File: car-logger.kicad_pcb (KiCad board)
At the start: 4 copper layers, 86.4 x 53.8 mm, 92 parts, among them J1 DB9_Male, J2 Conn_01x05, J3 USB_B_Micro, Q1 Q_NMOS_DGS, SW1 SW_Push, U1 STM32F042C6Tx, U2 S25FLxS, U3 TC122x, U4 MIC5504-3.3YM5, U5 TPS2662x, U6 TPS2662x, U7 TPS5516x-Q1, U8 ISOW1044, Y1 Crystal_GND24_Small

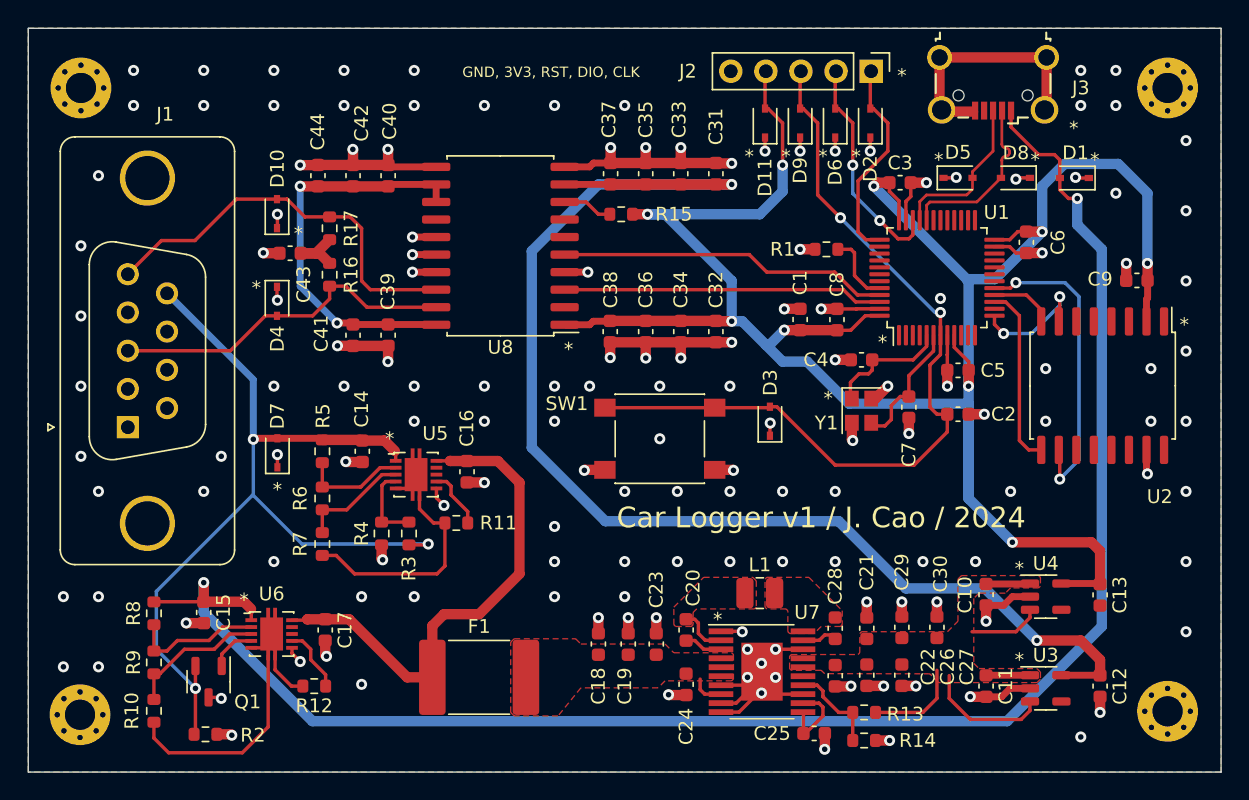
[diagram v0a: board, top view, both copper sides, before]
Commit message: Update tolerances, finish BOM
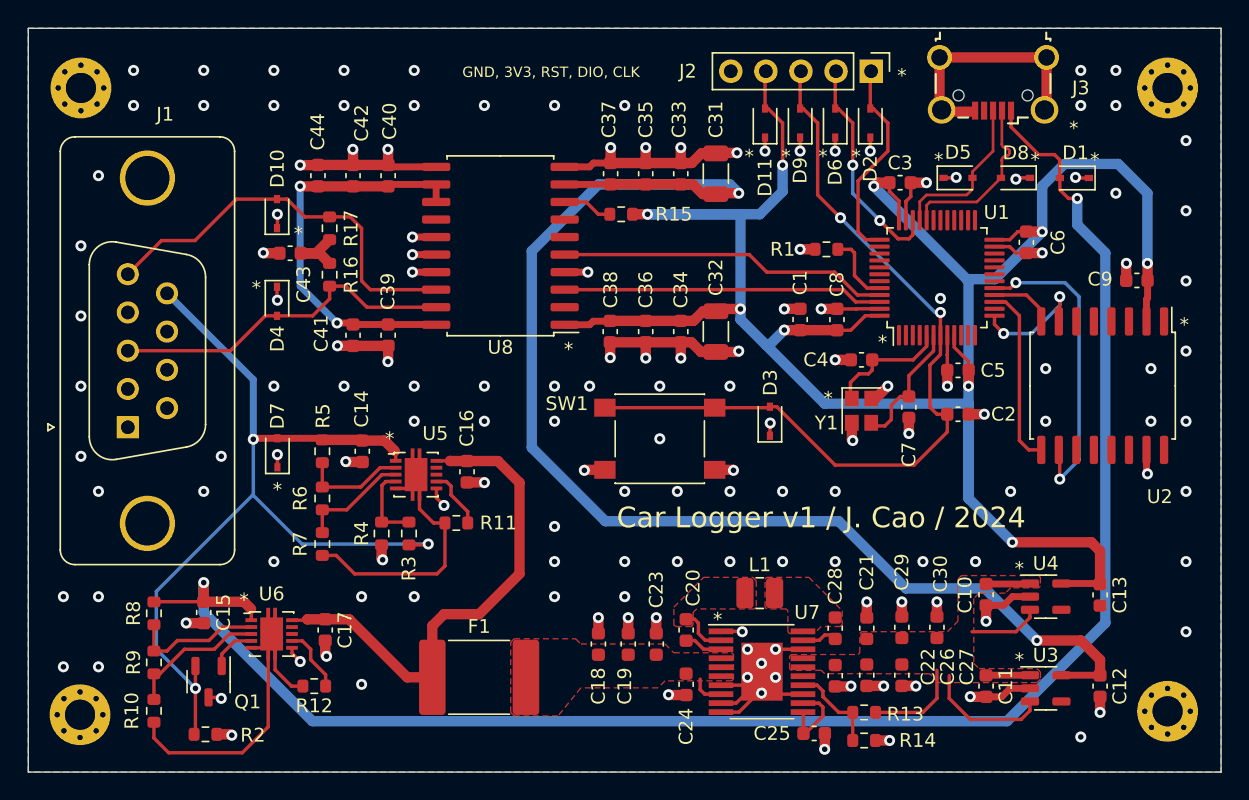
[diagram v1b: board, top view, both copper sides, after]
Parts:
- C31, C32: footprint Capacitor_SMD:C_0603_1608Metric -> Capacitor_SMD:C_1206_3216Metric
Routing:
- net +3V3: track 162.0 -> 165.8 mm
- net +5V: track 94.2 -> 95.8 mm
- net GND: track 137.6 -> 139.1 mm

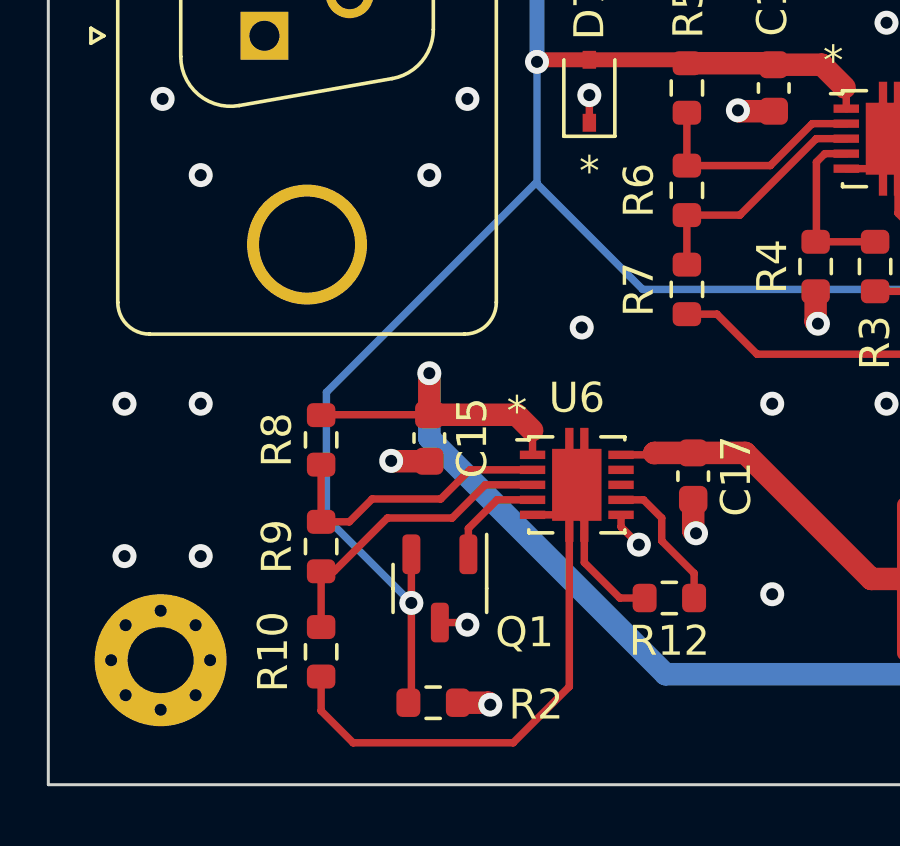
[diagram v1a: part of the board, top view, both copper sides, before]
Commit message: Correct error with FET pinout
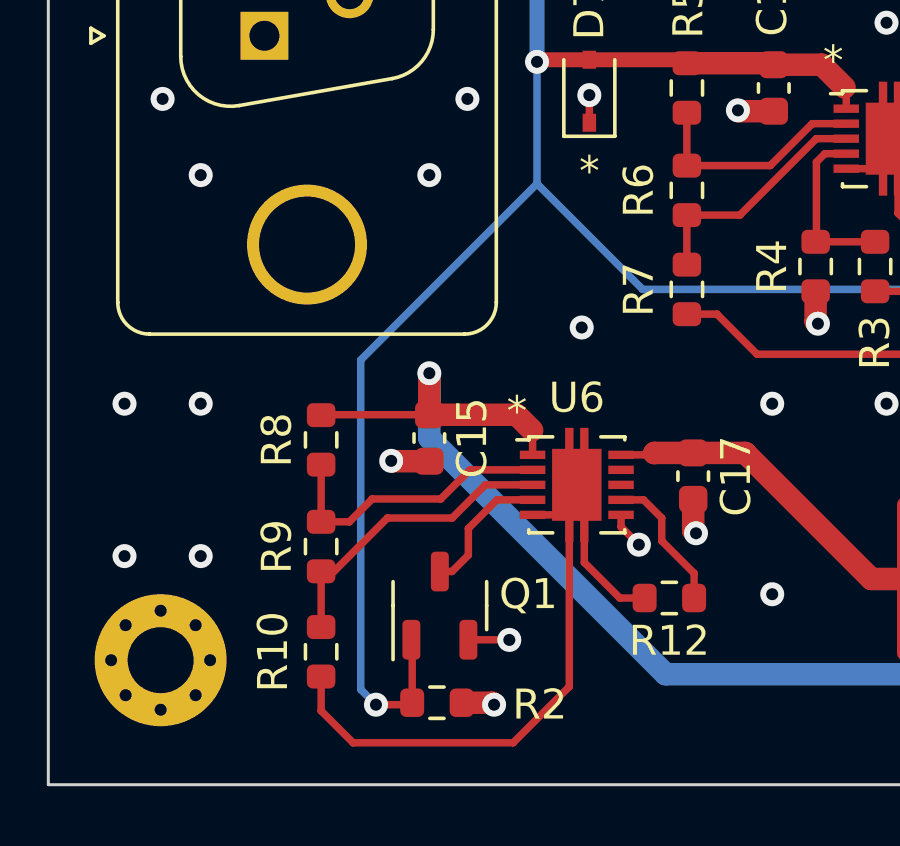
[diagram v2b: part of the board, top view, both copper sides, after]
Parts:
- Q1: value Q_NMOS_DGS -> Q_NMOS_GSD
- moved Q1 0.57 mm to (107.0, 105.8), turned to 90 degrees
- moved R2 0.13 mm to (106.9, 109.0)
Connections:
- Q1 pad 1: /Power/Protection and Switchover/PROT_VBUS_NSHDN -> +BATT
- Q1 pad 2: +BATT -> GND
- Q1 pad 3: GND -> /Power/Protection and Switchover/PROT_VBUS_NSHDN
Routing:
- net /Power/Protection and Switchover/PROT_VBUS_NSHDN: track 3.40 -> 4.60 mm

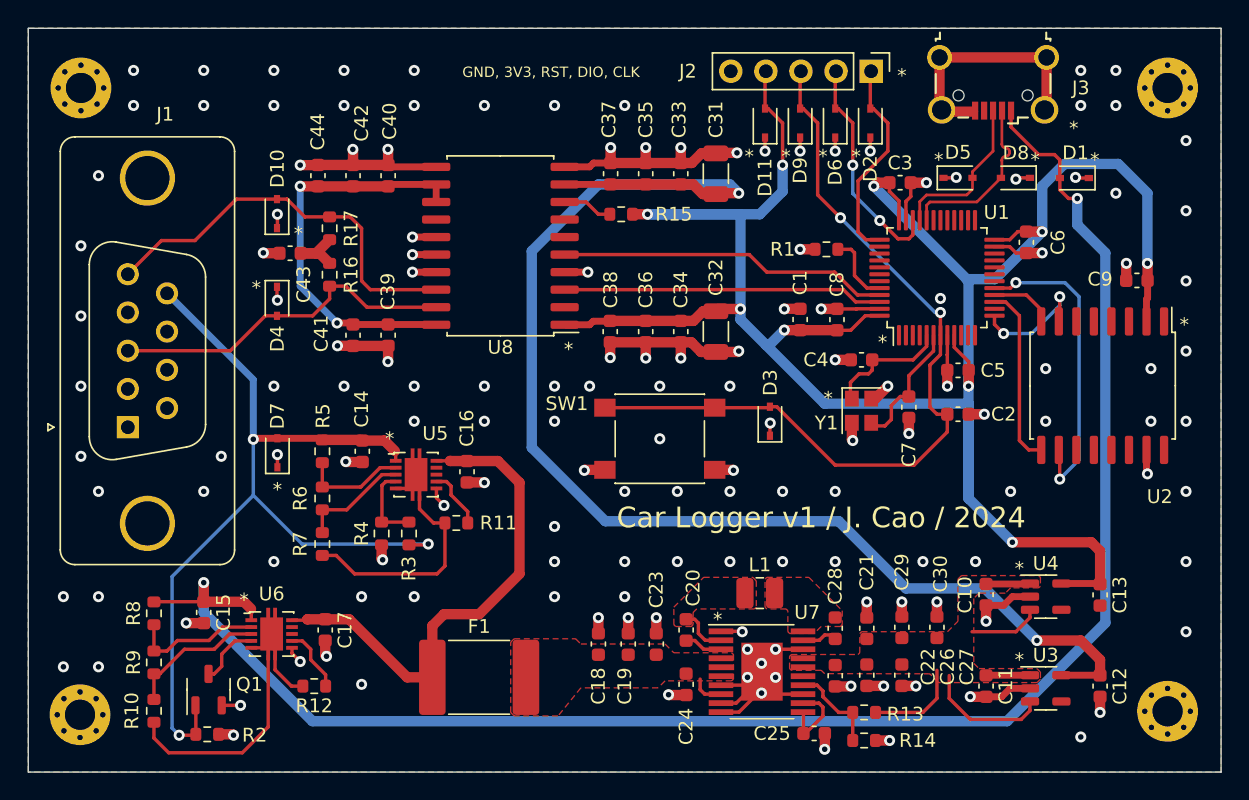
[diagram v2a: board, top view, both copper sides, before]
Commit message: Reduce GND flood top/bottom
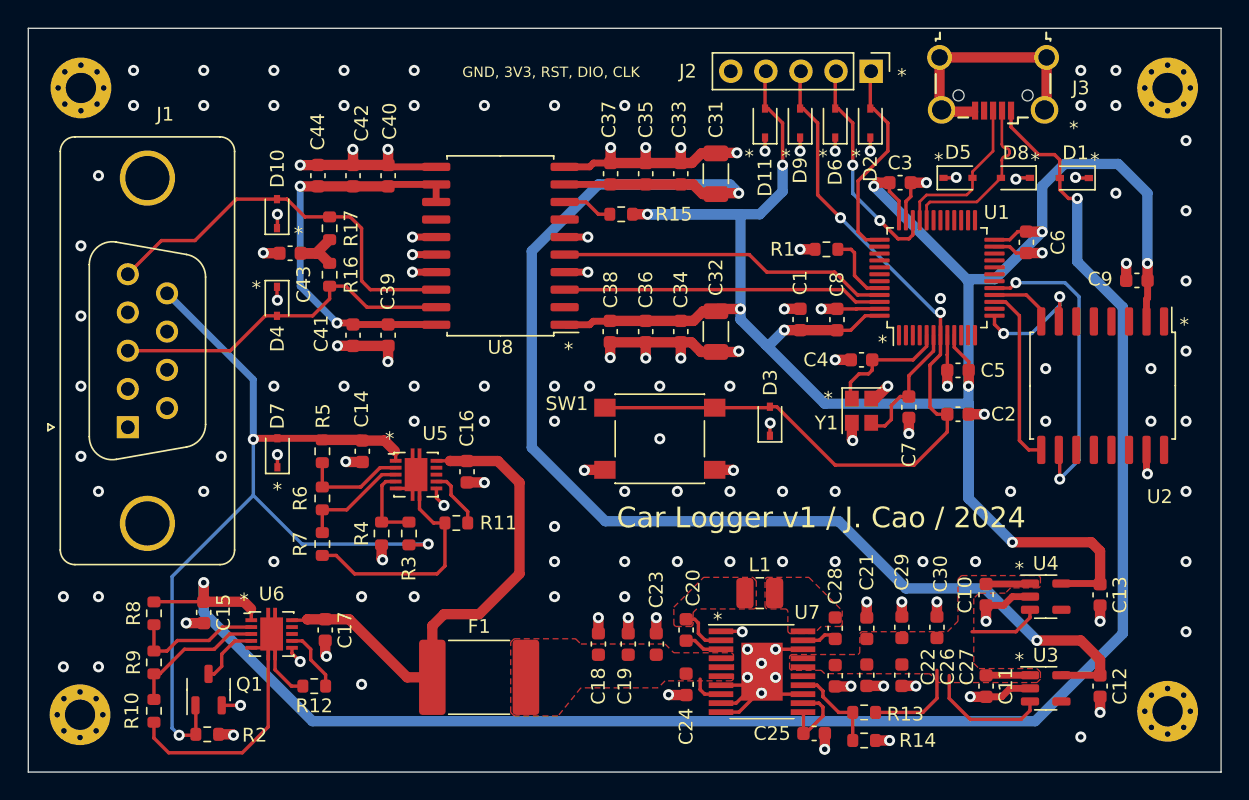
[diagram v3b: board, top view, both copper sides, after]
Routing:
- net GND: track 139.6 -> 142.4 mm, vias 143 -> 145
- net VBUS: track 124.0 -> 126.3 mm
- removed copper zone on B.Cu, net GND
- removed copper zone on F.Cu, net GND
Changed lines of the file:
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@@
     (fp_arc (start -9.885 -3.83) (mid -9.592107 -4.537107) (end -8.885 -4.83) (layer "F.Fab") (width 0.1))
     (fp_arc (start -8.885 7.67) (mid -9.592107 7.377107) (end -9.885 6.67) (layer "F.Fab") (width 0.1))
-    (fp_arc (start 12.459619 4.247837) (mid 11.912388 5.195671) (end 10.883927 5.57) (layer "F.Fab") (width 0.1))
+    (fp_arc (start 12.459619 4.247837) (mid 11.912387 5.19567) (end 10.883927 5.57) (layer "F.Fab") (width 0.1))
     (fp_arc (start 20.965 6.67) (mid 20.672107 7.377107) (end 19.965 7.67) (layer "F.Fab") (width 0.1))
     (pad "0" thru_hole circle (at -6.96 1.42 90) (size 4 4) (drill 3.2) (layers *.Cu *.Mask))
@@
   (segment (start 144.998 89.88) (end 145.034 89.916) (width 0.75) (layer "F.Cu") (net 2))
   (segment (start 153.53 81.915) (end 152.4 81.915) (width 0.75) (layer "F.Cu") (net 2))
+  (segment (start 132.81 73.025) (end 134.493 73.025) (width 0.5) (layer "F.Cu") (net 2))
   (segment (start 141.22 81.784) (end 141.224 81.788) (width 0.5) (layer "F.Cu") (net 2))
   (segment (start 165.494 74.181) (end 166.243 74.181) (width 0.25) (layer "F.Cu") (net 2))
@@
   (segment (start 141.22 67.66442) (end 142.01258 67.66442) (width 0.75) (layer "F.Cu") (net 2))
   (segment (start 125.743484 90.79071) (end 126.98571 90.79071) (width 0.75) (layer "F.Cu") (net 2))
+  (segment (start 171.577 99.708) (end 171.577 100.838) (width 0.75) (layer "F.Cu") (net 2))
   (segment (start 160.515 82.677) (end 160.515 83.807) (width 0.75) (layer "F.Cu") (net 2))
   (segment (start 108.773 109.027) (end 108.839 109.093) (width 0.75) (layer "F.Cu") (net 2))
@@
   (via (at 149.86 66.802) (size 0.8) (drill 0.4) (layers "F.Cu" "B.Cu") (net 2))
   (via (at 153.67 87.757) (size 0.8) (drill 0.4) (layers "F.Cu" "B.Cu") (net 2))
+  (via (at 171.577 100.838) (size 0.8) (drill 0.4) (layers "F.Cu" "B.Cu") (net 2))
   (via (at 172.72 63.5) (size 0.8) (drill 0.4) (layers "F.Cu" "B.Cu") (free) (net 2))
   (via (at 159.004 69.088) (size 0.8) (drill 0.4) (layers "F.Cu" "B.Cu") (net 2))
@@
   (via (at 127 90.805) (size 0.8) (drill 0.4) (layers "F.Cu" "B.Cu") (net 2))
   (via (at 149.86 73.914) (size 0.8) (drill 0.4) (layers "F.Cu" "B.Cu") (net 2))
+  (via (at 134.493 73.025) (size 0.8) (drill 0.4) (layers "F.Cu" "B.Cu") (net 2))
   (via (at 134.493 75.565) (size 0.8) (drill 0.4) (layers "F.Cu" "B.Cu") (net 2))
   (via (at 101.6 63.5) (size 0.8) (drill 0.4) (layers "F.Cu" "B.Cu") (free) (net 2))
@@
   (via (at 169.926 70.231) (size 0.8) (drill 0.4) (layers "F.Cu" "B.Cu") (net 8))
   (via (at 106.68 98.044) (size 0.8) (drill 0.4) (layers "F.Cu" "B.Cu") (net 8))
+  (segment (start 166.878 108.077) (end 114.554 108.077) (width 0.75) (layer "B.Cu") (net 8))
+  (segment (start 173.228 101.727) (end 166.878 108.077) (width 0.75) (layer "B.Cu") (net 8))
   (segment (start 114.554 108.077) (end 106.68 100.203) (width 0.75) (layer "B.Cu") (net 8))
-  (segment (start 171.958 74.168) (end 171.958 100.965) (width 0.75) (layer "B.Cu") (net 8))
+  (segment (start 173.228 78.105) (end 173.228 101.727) (width 0.75) (layer "B.Cu") (net 8))
+  (segment (start 169.926 70.231) (end 169.926 74.803) (width 0.75) (layer "B.Cu") (net 8))
+  (segment (start 169.926 74.803) (end 173.228 78.105) (width 0.75) (layer "B.Cu") (net 8))
   (segment (start 106.68 100.203) (end 106.68 98.044) (width 0.75) (layer "B.Cu") (net 8))
-  (segment (start 169.926 70.231) (end 169.926 72.136) (width 0.75) (layer "B.Cu") (net 8))
-  (segment (start 171.958 100.965) (end 164.846 108.077) (width 0.75) (layer "B.Cu") (net 8))
-  (segment (start 164.846 108.077) (end 114.554 108.077) (width 0.75) (layer "B.Cu") (net 8))
-  (segment (start 169.926 72.136) (end 171.958 74.168) (width 0.75) (layer "B.Cu") (net 8))
   (segment (start 114.1845 100.6995) (end 114.173 100.711) (width 0.75) (layer "F.Cu") (net 9))
   (segment (start 114.1195 100.7645) (end 114.173 100.711) (width 0.25) (layer "F.Cu") (net 9))
@@
   (segment (start 166.5025 100.01) (end 166.5025 100.5785) (width 0.25) (layer "F.Cu") (net 95))
   (segment (start 165.862 107.95) (end 162.179 107.95) (width 0.25) (layer "F.Cu") (net 95))
-  (zone (net 0) (net_name "") (layer "F.Cu") (hatch edge 0.508)
-    (connect_pads (clearance 0))
-    (min_thickness 0.254)
-    (keepout (tracks allowed) (vias allowed) (pads allowed) (copperpour not_allowed) (footprints allowed))
-    (fill (thermal_gap 0.508) (thermal_bridge_width 0.508))
-    (polygon
-      (pts
-        (xy 128.27 68.58)
-        (xy 128.27 78.74)
-        (xy 124.46 82.55)
-        (xy 110.49 82.55)
-        (xy 104.14 88.9)
-        (xy 100.33 88.9)
-        (xy 99.06 87.63)
-        (xy 99.06 74.93)
-        (xy 102.87 71.12)
-        (xy 106.68 71.12)
-        (xy 111.76 66.04)
-        (xy 125.73 66.04)
-      )
-    )
-  )
   (zone (net 12) (net_name "/Power/First Stage Buck Boost/BB_L1") (layer "F.Cu") (hatch edge 0.508)
     (priority 1)
@@
     )
   )
-  (zone (net 2) (net_name "GND") (layers "F.Cu" "In1.Cu" "In2.Cu" "B.Cu") (hatch edge 0.508)
-    (connect_pads yes (clearance 0.508))
-    (min_thickness 0.254) (filled_areas_thickness no)
-    (fill yes (thermal_gap 0.508) (thermal_bridge_width 0.508))
-    (polygon
-      (pts
-        (xy 180.34 111.76)
-        (xy 93.98 111.76)
-        (xy 93.98 57.912)
-        (xy 180.34 57.912)
-      )
-    )
-  )
   (zone (net 13) (net_name "/Power/First Stage Buck Boost/BB_L2") (layer "F.Cu") (hatch edge 0.508)
     (priority 1)
@@
       )
     )
+  )
+  (zone (net 2) (net_name "GND") (layers "In1.Cu" "In2.Cu") (hatch edge 0.508)
+    (connect_pads yes (clearance 0.508))
+    (min_thickness 0.254) (filled_areas_thickness no)
+    (fill yes (thermal_gap 0.508) (thermal_bridge_width 0.508))
+    (polygon
+      (pts
+        (xy 180.34 111.76)
+        (xy 93.98 111.76)
+        (xy 93.98 57.912)
+        (xy 180.34 57.912)
+      )
+    )
